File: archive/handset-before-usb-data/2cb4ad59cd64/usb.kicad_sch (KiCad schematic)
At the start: 4 parts, among them U17 TPD4E05U06DQAR

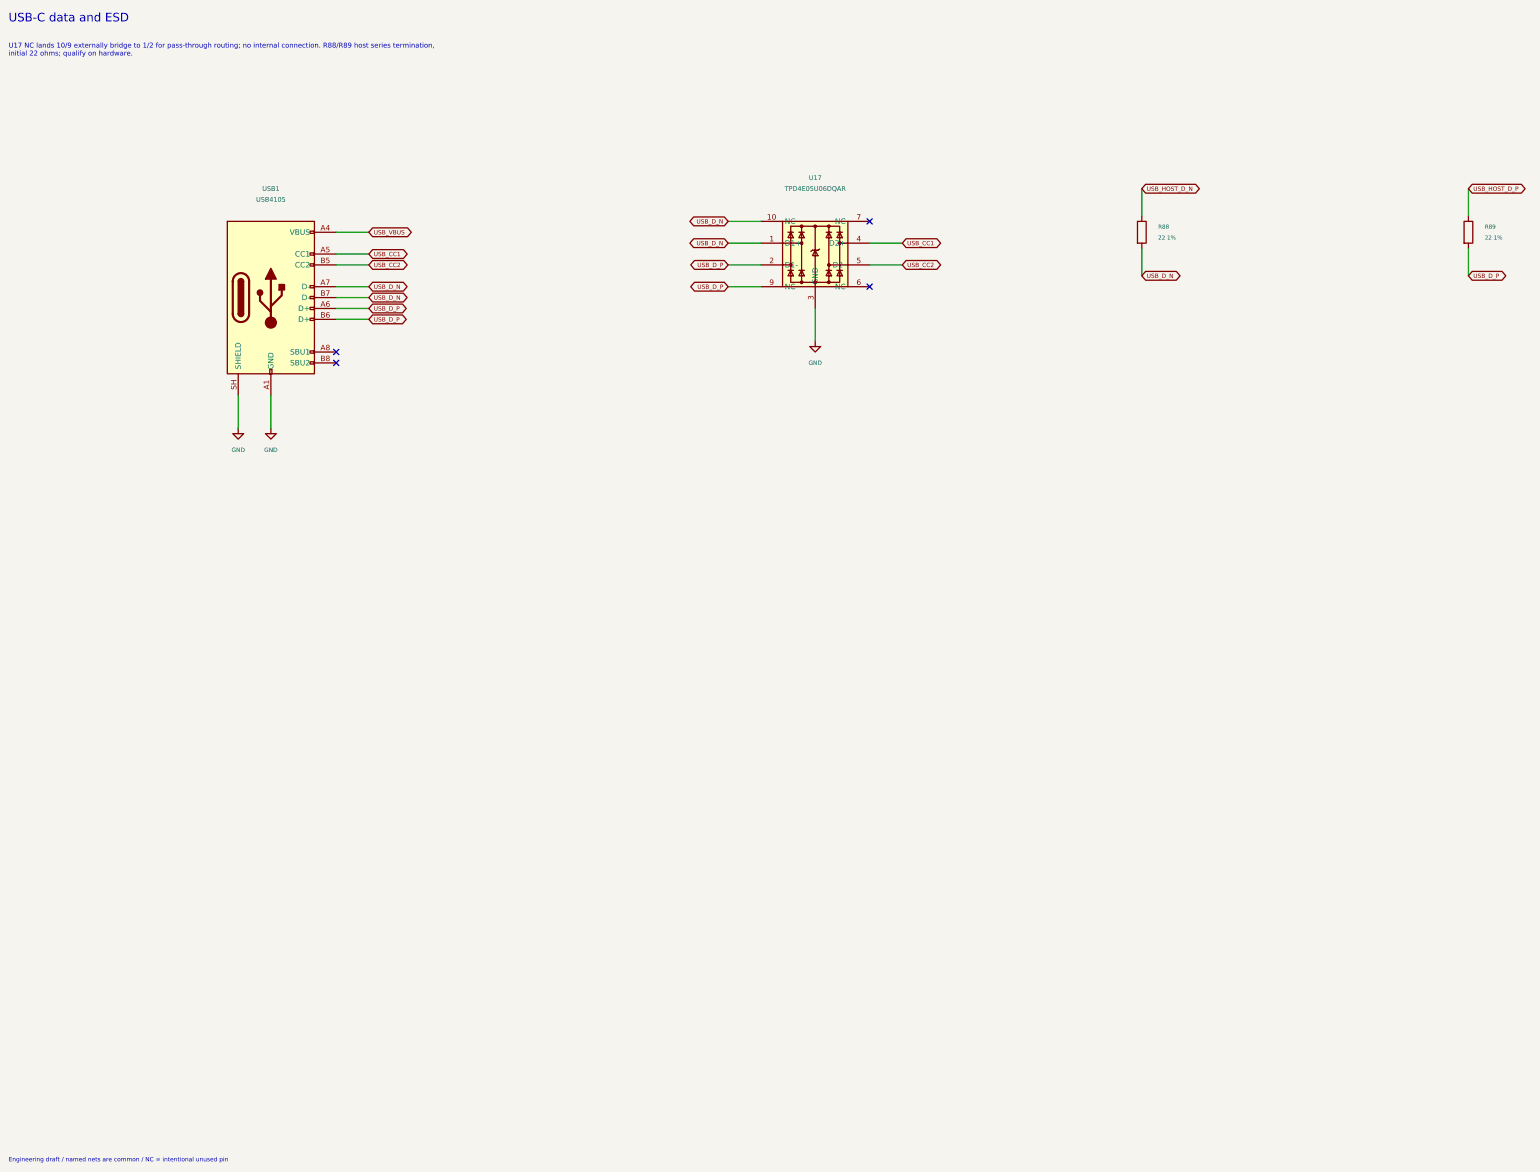
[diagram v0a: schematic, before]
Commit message: feat: route USB data and add termination
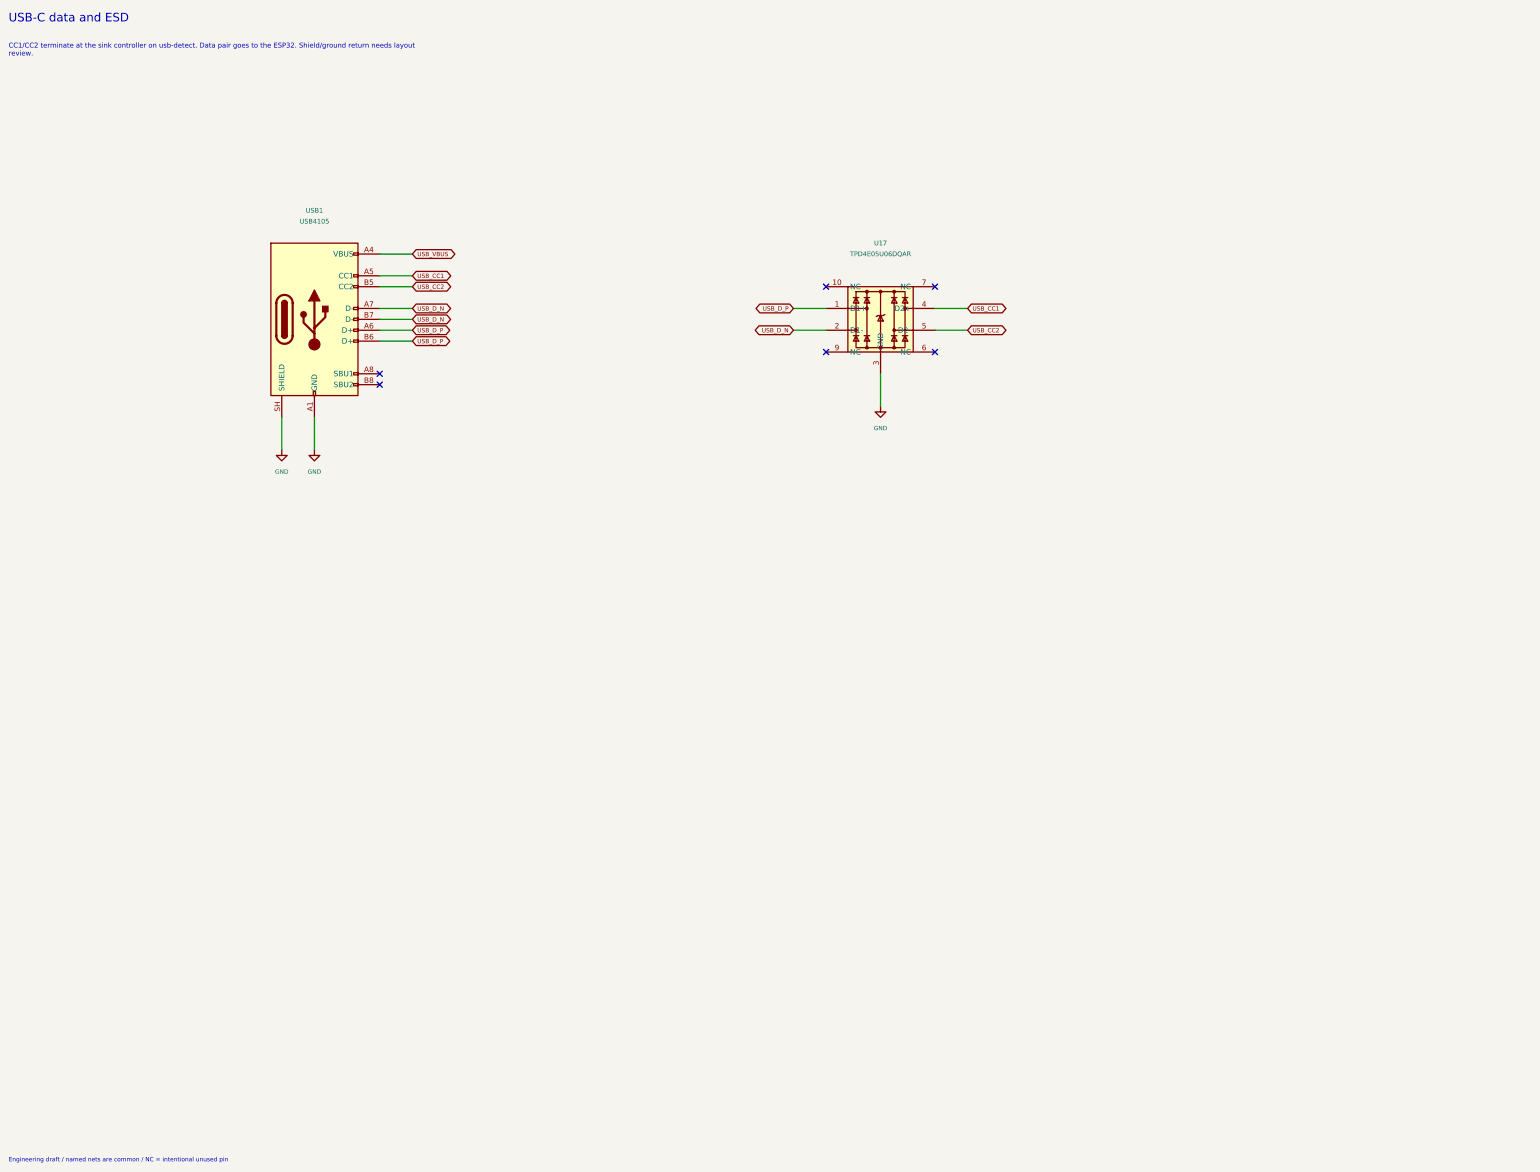
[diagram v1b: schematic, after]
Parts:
- removed R88, R89: 22 1%, Resistor_SMD:R_0402_1005Metric, symbol Device:R
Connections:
- net USB_D_N: now also U17.2 (D1-); no longer U17.1 (D1+), U17.10 (NC)
- net USB_D_P: now also U17.1 (D1+); no longer U17.2 (D1-), U17.9 (NC)
- no-connect marks 4 -> 6
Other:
- note added: "CC1/CC2 terminate at the sink controller on usb-detect. Data pair goes to the ESP32. Shield/ground return needs layout review."
- note removed: "U17 NC lands 10/9 externally bridge to 1/2 for pass-through routing; no internal connection. R88/R89 host series termination, initial 22 ohms; qualify on hardware."
- moved on the sheet: U17, USB1
